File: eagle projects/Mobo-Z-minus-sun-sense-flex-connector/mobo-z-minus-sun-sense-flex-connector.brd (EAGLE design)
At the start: 2 parts

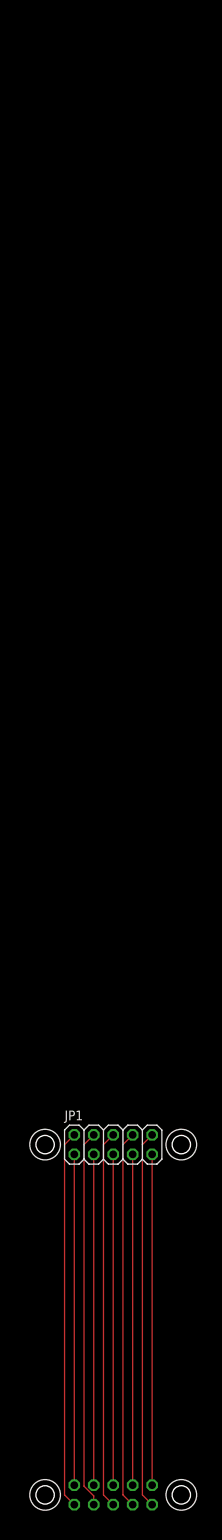
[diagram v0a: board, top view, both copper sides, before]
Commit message: Lengthened one of the flex connectors
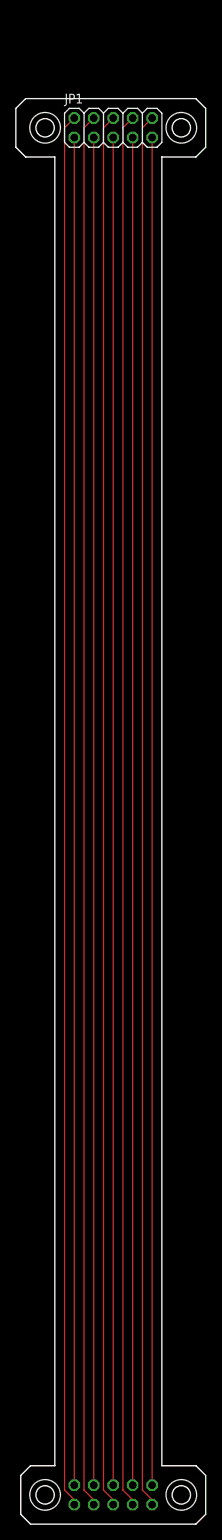
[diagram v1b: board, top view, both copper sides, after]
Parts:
- moved JP1 132.7 mm to (10.2, 178.4)
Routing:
- net N$5: track 49.3 -> 182.0 mm
- net N$4: track 49.3 -> 182.0 mm
- net N$3: track 49.3 -> 182.0 mm
- net N$2: track 49.3 -> 182.0 mm
- net N$1: track 49.3 -> 182.0 mm
- net N$9: track 43.2 -> 175.9 mm
- net N$8: track 43.2 -> 175.9 mm
- net N$7: track 43.2 -> 175.9 mm
- net N$6: track 43.2 -> 175.9 mm
- net N$10: track 43.2 -> 175.9 mm
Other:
- board outline added: 24.8 x 186.1 mm
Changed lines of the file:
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@@
 <board>
 <plain>
-<hole x="1.27" y="45.72" drill="2.4"/>
-<circle x="1.27" y="45.72" radius="2" width="0.1524" layer="21"/>
-<hole x="19.05" y="45.72" drill="2.4"/>
-<circle x="19.05" y="45.72" radius="2" width="0.1524" layer="21"/>
+<hole x="1.27" y="178.435" drill="2.4"/>
+<circle x="1.27" y="178.435" radius="2" width="0.1524" layer="21"/>
+<hole x="19.05" y="178.435" drill="2.4"/>
+<circle x="19.05" y="178.435" radius="2" width="0.1524" layer="21"/>
 <hole x="1.27" y="0" drill="2.4"/>
 <circle x="1.27" y="0" radius="2" width="0.1524" layer="21"/>
@@
 <circle x="19.05" y="0" radius="2" width="0.1524" layer="21"/>
 <text x="24.13" y="22.86" size="1.778" layer="48">need atleast 163.93 mm length</text>
+<dimension x1="-4.445" y1="1.905" x2="-4.445" y2="175.895" x3="-19.05" y3="88.9" textsize="1.778" layer="1"/>
+<wire x1="-1.905" y1="-2.54" x2="-1.905" y2="2.54" width="0.1524" layer="20"/>
+<wire x1="22.225" y1="2.54" x2="22.225" y2="-2.54" width="0.1524" layer="20"/>
+<wire x1="-2.54" y1="175.895" x2="-2.54" y2="180.975" width="0.1524" layer="20"/>
+<wire x1="22.225" y1="175.895" x2="22.225" y2="180.975" width="0.1524" layer="20"/>
+<wire x1="-2.54" y1="180.975" x2="-1.27" y2="182.245" width="0.1524" layer="20"/>
+<wire x1="-1.27" y1="182.245" x2="20.955" y2="182.245" width="0.1524" layer="20"/>
+<wire x1="20.955" y1="182.245" x2="22.225" y2="180.975" width="0.1524" layer="20"/>
+<wire x1="-2.54" y1="175.895" x2="-1.27" y2="174.625" width="0.1524" layer="20"/>
+<wire x1="22.225" y1="175.895" x2="20.955" y2="174.625" width="0.1524" layer="20"/>
+<wire x1="-1.905" y1="2.54" x2="-0.635" y2="3.81" width="0.1524" layer="20"/>
+<wire x1="-1.905" y1="-2.54" x2="-0.635" y2="-3.81" width="0.1524" layer="20"/>
+<wire x1="22.225" y1="2.54" x2="20.955" y2="3.81" width="0.1524" layer="20"/>
+<wire x1="22.225" y1="-2.54" x2="20.955" y2="-3.81" width="0.1524" layer="20"/>
+<wire x1="-0.635" y1="-3.81" x2="20.955" y2="-3.81" width="0.1524" layer="20"/>
+<wire x1="-0.635" y1="3.81" x2="2.54" y2="3.81" width="0.1524" layer="20"/>
+<wire x1="20.955" y1="3.81" x2="16.51" y2="3.81" width="0.1524" layer="20"/>
+<wire x1="-1.27" y1="174.625" x2="2.54" y2="174.625" width="0.1524" layer="20"/>
+<wire x1="20.955" y1="174.625" x2="16.51" y2="174.625" width="0.1524" layer="20"/>
+<wire x1="2.54" y1="174.625" x2="2.54" y2="3.81" width="0.1524" layer="20"/>
+<wire x1="16.51" y1="3.81" x2="16.51" y2="174.625" width="0.1524" layer="20"/>
 </plain>
 <attributes>
@@
 </autorouter>
 <elements>
-<element name="JP1" library="pinhead" library_urn="urn:adsk.eagle:library:325" package="2X05" package3d_urn="urn:adsk.eagle:package:22470/2" value="" x="10.16" y="45.72" smashed="yes">
-<attribute name="NAME" x="3.81" y="48.895" size="1.27" layer="25" ratio="10"/>
-<attribute name="POPULARITY" value="35" x="30.48" y="41.91" size="1.778" layer="27" display="off"/>
-<attribute name="VALUE" x="3.81" y="41.275" size="1.27" layer="27"/>
+<element name="JP1" library="pinhead" library_urn="urn:adsk.eagle:library:325" package="2X05" package3d_urn="urn:adsk.eagle:package:22470/2" value="" x="10.16" y="178.435" smashed="yes">
+<attribute name="NAME" x="3.81" y="181.61" size="1.27" layer="25" ratio="10"/>
+<attribute name="POPULARITY" value="35" x="30.48" y="174.625" size="1.778" layer="27" display="off"/>
+<attribute name="VALUE" x="3.81" y="173.99" size="1.27" layer="27"/>
 </element>
 <element name="JP2" library="pinhead" library_urn="urn:adsk.eagle:library:325" package="2X05" package3d_urn="urn:adsk.eagle:package:22470/2" value="" x="10.16" y="0" smashed="yes" rot="MR180">
@@
 <contactref element="JP1" pad="2"/>
 <contactref element="JP2" pad="2"/>
-<wire x1="5.08" y1="-1.27" x2="3.81" y2="0" width="0.1524" layer="1"/>
-<wire x1="3.81" y1="0" x2="3.81" y2="45.72" width="0.1524" layer="1"/>
-<wire x1="3.81" y1="45.72" x2="5.08" y2="46.99" width="0.1524" layer="1"/>
+<wire x1="3.81" y1="178.435" x2="3.81" y2="0.635" width="0.1524" layer="1"/>
+<wire x1="5.08" y1="-1.27" x2="5.08" y2="-0.635" width="0.1524" layer="1"/>
+<wire x1="5.08" y1="-0.635" x2="3.81" y2="0.635" width="0.1524" layer="1"/>
+<wire x1="3.81" y1="178.435" x2="5.08" y2="179.705" width="0.1524" layer="1"/>
 </signal>
 <signal name="N$2">
 <contactref element="JP1" pad="4"/>
 <contactref element="JP2" pad="4"/>
-<wire x1="7.62" y1="-0.130925" x2="7.62" y2="-1.27" width="0.1524" layer="1"/>
-<wire x1="7.62" y1="46.99" x2="6.35" y2="45.72" width="0.1524" layer="1"/>
-<wire x1="6.35" y1="45.72" x2="6.35" y2="1.139075" width="0.1524" layer="1"/>
-<wire x1="6.35" y1="1.139075" x2="7.62" y2="-0.130925" width="0.1524" layer="1"/>
+<wire x1="7.62" y1="179.705" x2="6.35" y2="178.435" width="0.1524" layer="1"/>
+<wire x1="6.35" y1="178.435" x2="6.35" y2="0.635" width="0.1524" layer="1"/>
+<wire x1="7.62" y1="-0.635" x2="7.62" y2="-1.27" width="0.1524" layer="1"/>
+<wire x1="7.62" y1="-0.635" x2="6.35" y2="0.635" width="0.1524" layer="1"/>
 </signal>
 <signal name="N$3">
 <contactref element="JP1" pad="6"/>
 <contactref element="JP2" pad="6"/>
-<wire x1="10.16" y1="-1.27" x2="8.89" y2="0" width="0.1524" layer="1"/>
-<wire x1="8.89" y1="45.72" x2="10.16" y2="46.99" width="0.1524" layer="1"/>
-<wire x1="8.89" y1="0" x2="8.89" y2="45.72" width="0.1524" layer="1"/>
+<wire x1="8.89" y1="178.435" x2="10.16" y2="179.705" width="0.1524" layer="1"/>
+<wire x1="8.89" y1="178.435" x2="8.89" y2="0.635" width="0.1524" layer="1"/>
+<wire x1="10.16" y1="-1.27" x2="10.16" y2="-0.635" width="0.1524" layer="1"/>
+<wire x1="10.16" y1="-0.635" x2="8.89" y2="0.635" width="0.1524" layer="1"/>
 </signal>
 <signal name="N$4">
 <contactref element="JP1" pad="8"/>
 <contactref element="JP2" pad="8"/>
-<wire x1="12.7" y1="-1.27" x2="11.43" y2="0" width="0.1524" layer="1"/>
-<wire x1="11.43" y1="45.72" x2="12.7" y2="46.99" width="0.1524" layer="1"/>
-<wire x1="11.43" y1="0" x2="11.43" y2="45.72" width="0.1524" layer="1"/>
+<wire x1="11.43" y1="178.435" x2="12.7" y2="179.705" width="0.1524" layer="1"/>
+<wire x1="11.43" y1="178.435" x2="11.43" y2="0.635" width="0.1524" layer="1"/>
+<wire x1="12.7" y1="-1.27" x2="12.7" y2="-0.635" width="0.1524" layer="1"/>
+<wire x1="12.7" y1="-0.635" x2="11.43" y2="0.635" width="0.1524" layer="1"/>
 </signal>
 <signal name="N$5">
 <contactref element="JP1" pad="10"/>
 <contactref element="JP2" pad="10"/>
-<wire x1="15.24" y1="-1.27" x2="13.97" y2="0" width="0.1524" layer="1"/>
-<wire x1="13.97" y1="45.72" x2="15.24" y2="46.99" width="0.1524" layer="1"/>
-<wire x1="13.97" y1="0" x2="13.97" y2="45.72" width="0.1524" layer="1"/>
+<wire x1="13.97" y1="178.435" x2="15.24" y2="179.705" width="0.1524" layer="1"/>
+<wire x1="13.97" y1="178.435" x2="13.97" y2="0.635" width="0.1524" layer="1"/>
+<wire x1="15.24" y1="-1.27" x2="15.24" y2="-0.635" width="0.1524" layer="1"/>
+<wire x1="15.24" y1="-0.635" x2="13.97" y2="0.635" width="0.1524" layer="1"/>
 </signal>
 <signal name="N$6">
 <contactref element="JP1" pad="1"/>
 <contactref element="JP2" pad="1"/>
-<wire x1="5.08" y1="44.45" x2="5.08" y2="1.27" width="0.1524" layer="1"/>
+<wire x1="5.08" y1="177.165" x2="5.08" y2="1.27" width="0.1524" layer="1"/>
 </signal>
 <signal name="N$7">
 <contactref element="JP1" pad="3"/>
 <contactref element="JP2" pad="3"/>
-<wire x1="7.62" y1="1.27" x2="7.62" y2="44.45" width="0.1524" layer="1"/>
+<wire x1="7.62" y1="177.165" x2="7.62" y2="1.27" width="0.1524" layer="1"/>
 </signal>
 <signal name="N$8">
 <contactref element="JP2" pad="5"/>
 <contactref element="JP1" pad="5"/>
-<wire x1="10.16" y1="1.27" x2="10.16" y2="44.45" width="0.1524" layer="1"/>
+<wire x1="10.16" y1="177.165" x2="10.16" y2="1.27" width="0.1524" layer="1"/>
 </signal>
 <signal name="N$9">
 <contactref element="JP1" pad="7"/>
 <contactref element="JP2" pad="7"/>
-<wire x1="12.7" y1="1.27" x2="12.7" y2="44.45" width="0.1524" layer="1"/>
+<wire x1="12.7" y1="177.165" x2="12.7" y2="1.27" width="0.1524" layer="1"/>
 </signal>
 <signal name="N$10">
 <contactref element="JP1" pad="9"/>
 <contactref element="JP2" pad="9"/>
-<wire x1="15.24" y1="1.27" x2="15.24" y2="44.45" width="0.1524" layer="1"/>
+<wire x1="15.24" y1="177.165" x2="15.24" y2="1.27" width="0.1524" layer="1"/>
 </signal>
 </signals>

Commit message: Created 5x2 SMD 2.54mm footprint and added it to board that needs it
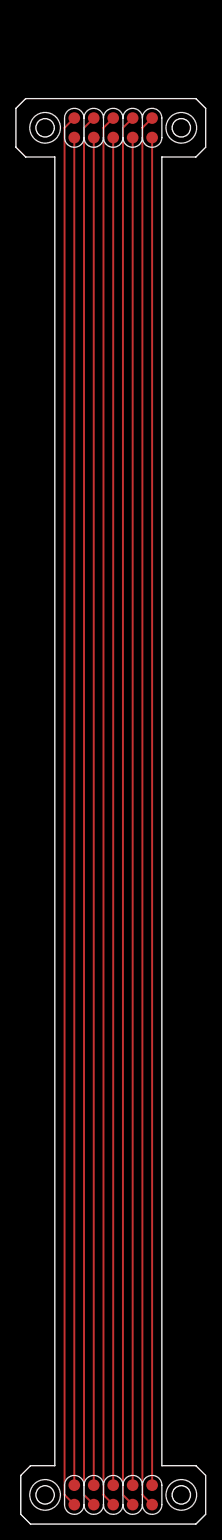
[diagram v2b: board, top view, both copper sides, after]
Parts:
- removed JP1, JP2: (no value), pinhead:2X05
- added X1, X2: 5X2_SMD_2.54MM_HEADER, SMD_headers:5X2_HEADER
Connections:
- net N$1: now also X1.P6, X2.P10; no longer JP1.2, JP2.2
- net N$10: now also X1.P5, X2.P1; no longer JP1.9, JP2.9
- net N$2: now also X1.P7, X2.P9; no longer JP1.4, JP2.4
- net N$3: now also X1.P8, X2.P8; no longer JP1.6, JP2.6
- net N$4: now also X1.P9, X2.P7; no longer JP1.8, JP2.8
- net N$5: now also X1.P10, X2.P6; no longer JP1.10, JP2.10
- net N$6: now also X1.P1, X2.P5; no longer JP1.1, JP2.1
- net N$7: now also X1.P2, X2.P4; no longer JP1.3, JP2.3
- net N$8: now also X1.P3, X2.P3; no longer JP1.5, JP2.5
- net N$9: now also X1.P4, X2.P2; no longer JP1.7, JP2.7
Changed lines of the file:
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@@
 </autorouter>
 <elements>
-<element name="JP1" library="pinhead" library_urn="urn:adsk.eagle:library:325" package="2X05" package3d_urn="urn:adsk.eagle:package:22470/2" value="" x="10.16" y="178.435" smashed="yes">
-<attribute name="NAME" x="3.81" y="181.61" size="1.27" layer="25" ratio="10"/>
-<attribute name="POPULARITY" value="35" x="30.48" y="174.625" size="1.778" layer="27" display="off"/>
-<attribute name="VALUE" x="3.81" y="173.99" size="1.27" layer="27"/>
-</element>
-<element name="JP2" library="pinhead" library_urn="urn:adsk.eagle:library:325" package="2X05" package3d_urn="urn:adsk.eagle:package:22470/2" value="" x="10.16" y="0" smashed="yes" rot="MR180">
-<attribute name="NAME" x="3.81" y="-3.175" size="1.27" layer="26" ratio="10" rot="MR180"/>
-<attribute name="POPULARITY" value="35" x="30.48" y="11.43" size="1.778" layer="28" rot="MR180" display="off"/>
-<attribute name="VALUE" x="3.81" y="4.445" size="1.27" layer="28" rot="MR180"/>
-</element>
+<element name="X1" library="SMD_headers" package="5X2_HEADER" value="5X2_SMD_2.54MM_HEADER" x="10.16" y="178.435" smashed="yes" rot="R180"/>
+<element name="X2" library="SMD_headers" package="5X2_HEADER" value="5X2_SMD_2.54MM_HEADER" x="10.16" y="0" smashed="yes"/>
 </elements>
 <signals>
+<signal name="N$6">
+<contactref element="X1" pad="P1"/>
+<contactref element="X2" pad="P5"/>
+<wire x1="5.08" y1="177.165" x2="5.08" y2="1.27" width="0.254" layer="1"/>
+</signal>
+<signal name="N$7">
+<contactref element="X1" pad="P2"/>
+<contactref element="X2" pad="P4"/>
+<wire x1="7.62" y1="1.27" x2="7.62" y2="176.53" width="0.254" layer="1"/>
+<wire x1="7.62" y1="176.53" x2="8.255" y2="177.165" width="0.254" layer="1"/>
+<wire x1="8.255" y1="177.165" x2="7.62" y2="177.165" width="0" layer="19" extent="1-1"/>
+</signal>
+<signal name="N$8">
+<contactref element="X1" pad="P3"/>
+<contactref element="X2" pad="P3"/>
+<wire x1="10.16" y1="177.165" x2="10.16" y2="1.27" width="0.254" layer="1"/>
+</signal>
+<signal name="N$9">
+<contactref element="X1" pad="P4"/>
+<contactref element="X2" pad="P2"/>
+<wire x1="12.7" y1="1.27" x2="12.7" y2="177.165" width="0.254" layer="1"/>
+</signal>
+<signal name="N$10">
+<contactref element="X1" pad="P5"/>
+<contactref element="X2" pad="P1"/>
+<wire x1="15.24" y1="177.165" x2="15.24" y2="1.27" width="0.254" layer="1"/>
+</signal>
 <signal name="N$1">
-<contactref element="JP1" pad="2"/>
-<contactref element="JP2" pad="2"/>
-<wire x1="3.81" y1="178.435" x2="3.81" y2="0.635" width="0.1524" layer="1"/>
-<wire x1="5.08" y1="-1.27" x2="5.08" y2="-0.635" width="0.1524" layer="1"/>
-<wire x1="5.08" y1="-0.635" x2="3.81" y2="0.635" width="0.1524" layer="1"/>
-<wire x1="3.81" y1="178.435" x2="5.08" y2="179.705" width="0.1524" layer="1"/>
+<contactref element="X1" pad="P6"/>
+<contactref element="X2" pad="P10"/>
+<wire x1="5.08" y1="-1.27" x2="3.81" y2="0" width="0.254" layer="1"/>
+<wire x1="3.81" y1="0" x2="3.81" y2="178.435" width="0.254" layer="1"/>
+<wire x1="3.81" y1="178.435" x2="5.08" y2="179.705" width="0.254" layer="1"/>
 </signal>
 <signal name="N$2">
-<contactref element="JP1" pad="4"/>
-<contactref element="JP2" pad="4"/>
-<wire x1="7.62" y1="179.705" x2="6.35" y2="178.435" width="0.1524" layer="1"/>
-<wire x1="6.35" y1="178.435" x2="6.35" y2="0.635" width="0.1524" layer="1"/>
-<wire x1="7.62" y1="-0.635" x2="7.62" y2="-1.27" width="0.1524" layer="1"/>
-<wire x1="7.62" y1="-0.635" x2="6.35" y2="0.635" width="0.1524" layer="1"/>
+<contactref element="X1" pad="P7"/>
+<contactref element="X2" pad="P9"/>
+<wire x1="7.62" y1="179.705" x2="6.35" y2="178.435" width="0.254" layer="1"/>
+<wire x1="6.35" y1="178.435" x2="6.35" y2="0" width="0.254" layer="1"/>
+<wire x1="6.35" y1="0" x2="7.62" y2="-1.27" width="0.254" layer="1"/>
 </signal>
 <signal name="N$3">
-<contactref element="JP1" pad="6"/>
-<contactref element="JP2" pad="6"/>
-<wire x1="8.89" y1="178.435" x2="10.16" y2="179.705" width="0.1524" layer="1"/>
-<wire x1="8.89" y1="178.435" x2="8.89" y2="0.635" width="0.1524" layer="1"/>
-<wire x1="10.16" y1="-1.27" x2="10.16" y2="-0.635" width="0.1524" layer="1"/>
-<wire x1="10.16" y1="-0.635" x2="8.89" y2="0.635" width="0.1524" layer="1"/>
+<contactref element="X1" pad="P8"/>
+<contactref element="X2" pad="P8"/>
+<wire x1="10.16" y1="-1.27" x2="8.89" y2="0" width="0.254" layer="1"/>
+<wire x1="8.89" y1="0" x2="8.89" y2="178.435" width="0.254" layer="1"/>
+<wire x1="8.89" y1="178.435" x2="10.16" y2="179.705" width="0.254" layer="1"/>
 </signal>
 <signal name="N$4">
-<contactref element="JP1" pad="8"/>
-<contactref element="JP2" pad="8"/>
-<wire x1="11.43" y1="178.435" x2="12.7" y2="179.705" width="0.1524" layer="1"/>
-<wire x1="11.43" y1="178.435" x2="11.43" y2="0.635" width="0.1524" layer="1"/>
-<wire x1="12.7" y1="-1.27" x2="12.7" y2="-0.635" width="0.1524" layer="1"/>
-<wire x1="12.7" y1="-0.635" x2="11.43" y2="0.635" width="0.1524" layer="1"/>
+<contactref element="X1" pad="P9"/>
+<contactref element="X2" pad="P7"/>
+<wire x1="12.7" y1="179.705" x2="11.43" y2="178.435" width="0.254" layer="1"/>
+<wire x1="11.43" y1="178.435" x2="11.43" y2="0" width="0.254" layer="1"/>
+<wire x1="12.7" y1="-1.27" x2="11.43" y2="0" width="0.254" layer="1"/>
 </signal>
 <signal name="N$5">
-<contactref element="JP1" pad="10"/>
-<contactref element="JP2" pad="10"/>
-<wire x1="13.97" y1="178.435" x2="15.24" y2="179.705" width="0.1524" layer="1"/>
-<wire x1="13.97" y1="178.435" x2="13.97" y2="0.635" width="0.1524" layer="1"/>
-<wire x1="15.24" y1="-1.27" x2="15.24" y2="-0.635" width="0.1524" layer="1"/>
-<wire x1="15.24" y1="-0.635" x2="13.97" y2="0.635" width="0.1524" layer="1"/>
-</signal>
-<signal name="N$6">
-<contactref element="JP1" pad="1"/>
-<contactref element="JP2" pad="1"/>
-<wire x1="5.08" y1="177.165" x2="5.08" y2="1.27" width="0.1524" layer="1"/>
-</signal>
-<signal name="N$7">
-<contactref element="JP1" pad="3"/>
-<contactref element="JP2" pad="3"/>
-<wire x1="7.62" y1="177.165" x2="7.62" y2="1.27" width="0.1524" layer="1"/>
-</signal>
-<signal name="N$8">
-<contactref element="JP2" pad="5"/>
-<contactref element="JP1" pad="5"/>
-<wire x1="10.16" y1="177.165" x2="10.16" y2="1.27" width="0.1524" layer="1"/>
-</signal>
-<signal name="N$9">
-<contactref element="JP1" pad="7"/>
-<contactref element="JP2" pad="7"/>
-<wire x1="12.7" y1="177.165" x2="12.7" y2="1.27" width="0.1524" layer="1"/>
-</signal>
-<signal name="N$10">
-<contactref element="JP1" pad="9"/>
-<contactref element="JP2" pad="9"/>
-<wire x1="15.24" y1="177.165" x2="15.24" y2="1.27" width="0.1524" layer="1"/>
+<contactref element="X1" pad="P10"/>
+<contactref element="X2" pad="P6"/>
+<wire x1="15.24" y1="-1.27" x2="13.97" y2="0" width="0.254" layer="1"/>
+<wire x1="13.97" y1="178.435" x2="15.24" y2="179.705" width="0.254" layer="1"/>
+<wire x1="13.97" y1="0" x2="13.97" y2="178.435" width="0.254" layer="1"/>
 </signal>
 </signals>
@@
 </board>
 </drawing>
-<compatibility>
-<note version="8.2" severity="warning">
-Since Version 8.2, EAGLE supports online libraries. The ids
-of those online libraries will not be understood (or retained)
-with this version.
-</note>
-<note version="8.3" severity="warning">
-Since Version 8.3, EAGLE supports URNs for individual library
-assets (packages, symbols, and devices). The URNs of those assets
-will not be understood (or retained) with this version.
-</note>
-<note version="8.3" severity="warning">
-Since Version 8.3, EAGLE supports the association of 3D packages
-with devices in libraries, schematics, and board files. Those 3D
-packages will not be understood (or retained) with this version.
-</note>
-</compatibility>
 </eagle>
